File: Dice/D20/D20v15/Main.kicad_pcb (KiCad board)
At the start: 2 copper layers, 101.9 x 44.5 mm, 84 parts, among them J1 Conn_01x14, J2 Conn_01x04, J3 Conn_01x02, J4 DNP, P5 COILA, P6 COILB, U1 N52810_QFN32, U2 KXTJ3-1057, U3 PJ75AL50SA, U4 ME6215, U5 MCP73832T-2ACI/OT, U6 MT9700, U7 74AHC1G08, U8 TMR1366, Y1 32MHz 40ppm

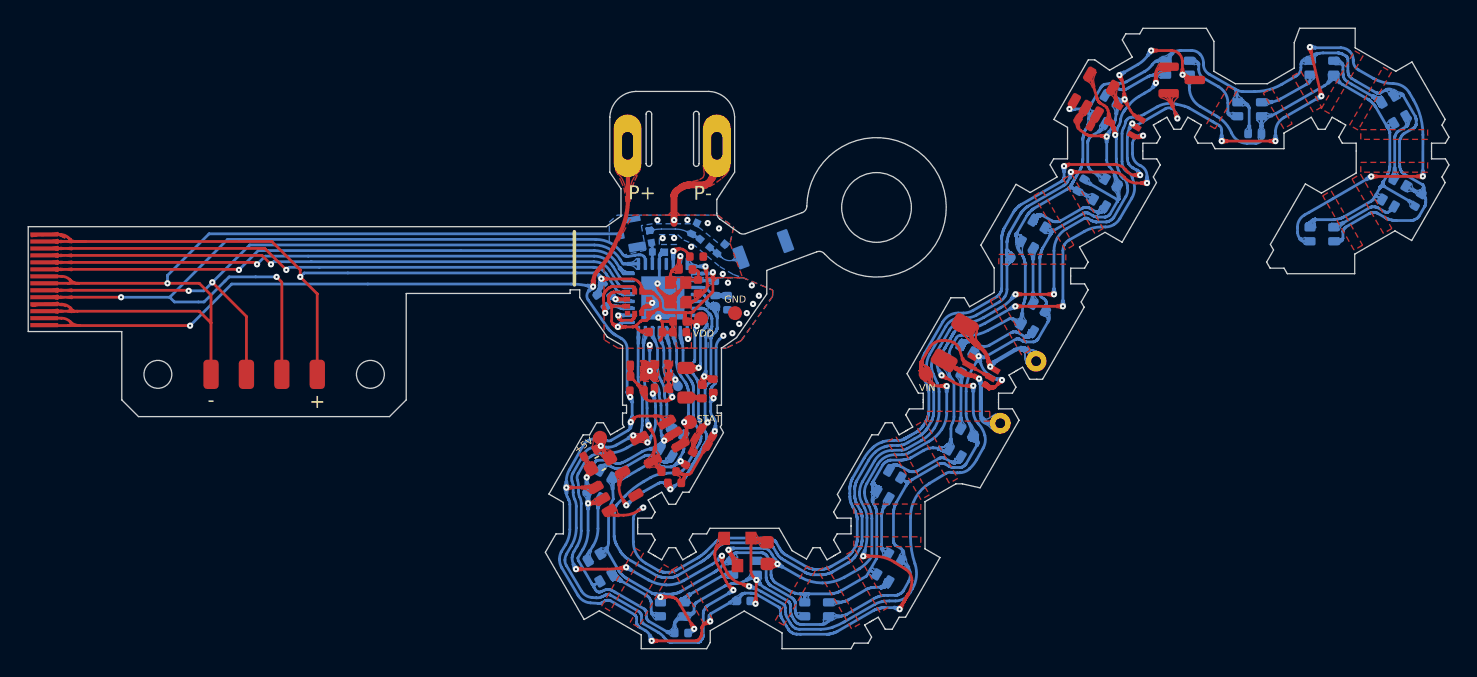
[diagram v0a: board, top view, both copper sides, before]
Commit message: Update D20V15 to include NTC over battery
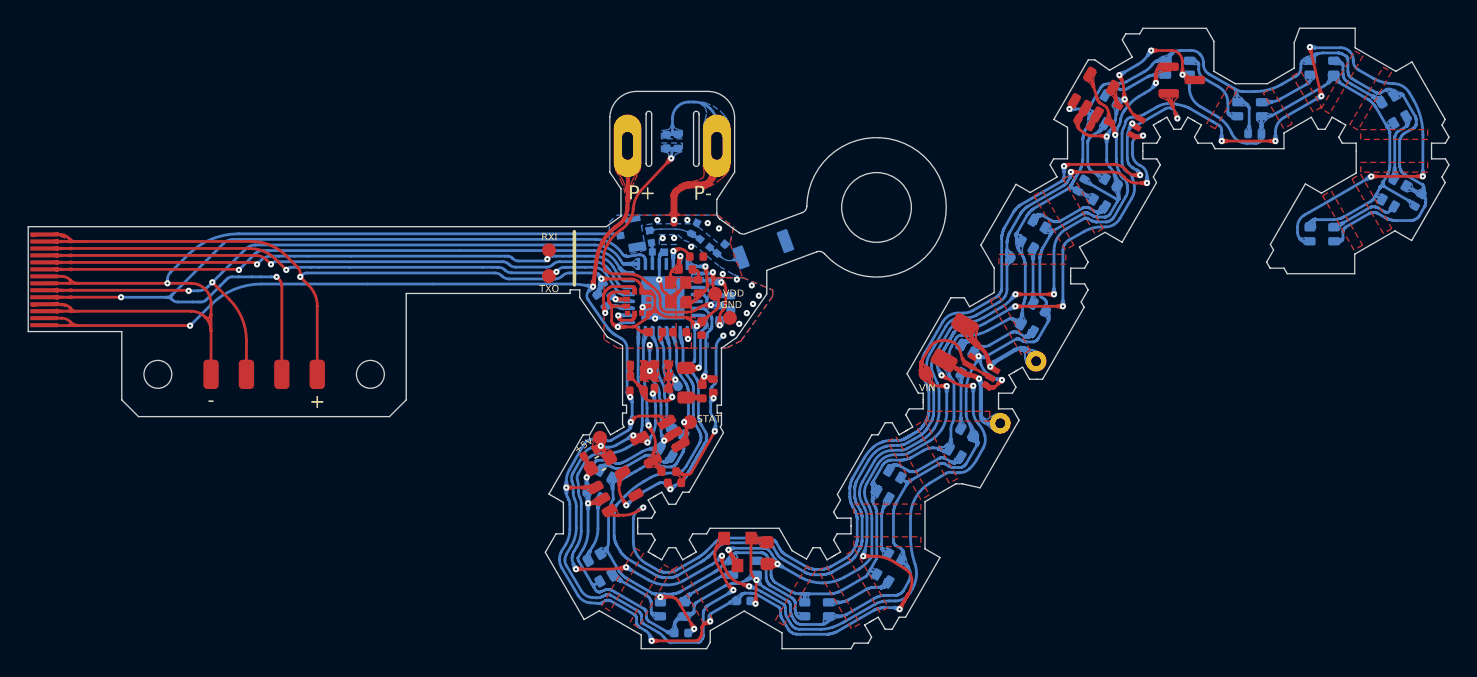
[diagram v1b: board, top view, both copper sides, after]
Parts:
- removed R13: 4.02M 1%, Pixels-dice:R_0402_1005Metric
- removed R14: 10M 1%, Pixels-dice:R_0402_1005Metric
- removed W12: VLED_S, Pixels-dice:TEST_PIN
- added R5: 100k 1%, Pixels-dice:R_0402_1005Metric, B.Cu at (145.8, 89.5)
- added TH1: NTC 100k @ 25C, Pixels-dice:R_0402_1005Metric, B.Cu at (142.8, 77.2)
- added W1: RXI, Pixels-dice:TEST_PIN, F.Cu at (133.5, 85.0)
- added W2: TXO, Pixels-dice:TEST_PIN, F.Cu at (133.5, 86.8)
- C6: value 10nF 25V 10% -> 0.1uF 10V 20%; moved to B.Cu
- moved C6 21.1 mm to (142.0, 77.2), turned to 90 degrees
- moved W25 2.04 mm to (145.5, 88.1)
- moved C4 1.64 mm to (144.5, 90.6), turned to -90 degrees
- moved W19 0.50 mm to (146.5, 89.8)
- moved R9 0.24 mm to (146.6, 88.8)
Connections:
- net /VLED_SENSE renamed /BATT_NTC
- net Net-(R10-Pad2) renamed /NTC_ID_VDD
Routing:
- net /BATT_NTC: track 12.8 -> 22.8 mm, vias 1 -> 2
- net GND: track 281.8 -> 287.9 mm
- net /NTC_ID_VDD: track 1.29 -> 4.99 mm, vias 0 -> 2
- net VDD: track 100.6 -> 99.3 mm
- net VDC: track 148.2 -> 147.4 mm, vias 4 -> 3
- net RXI: track 43.0 -> 43.1 mm, vias 1 -> 2
- net TXO: track 43.5 -> 43.6 mm, vias 1 -> 2
- added copper zone on B.Cu, net /BATT_NTC
- added copper zone on F.Cu, net /BATT_NTC
- added copper zone on B.Cu, net /NTC_ID_VDD
- added copper zone on F.Cu, net /NTC_ID_VDD
- added copper zone on B.Cu, net VDD
- added copper zone on F.Cu, net VDD

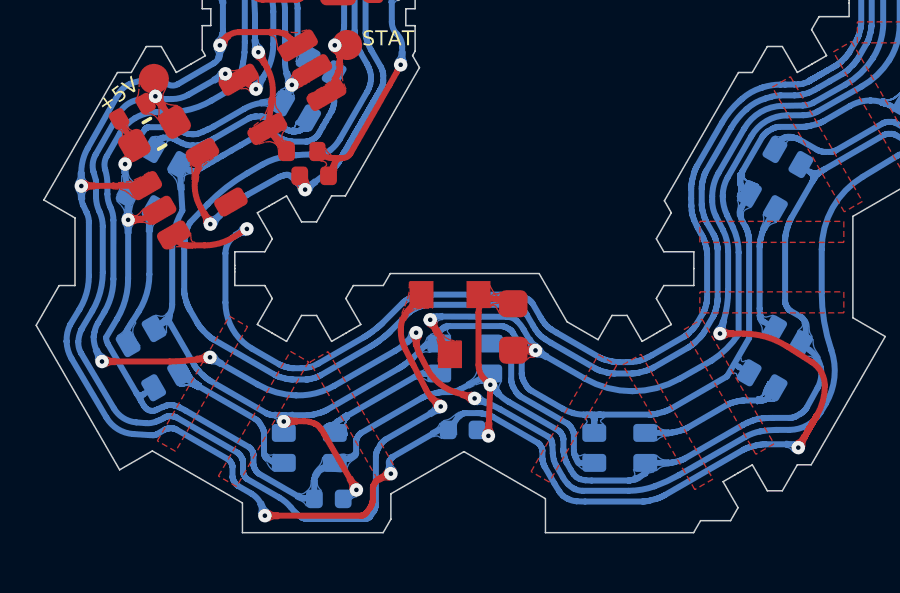
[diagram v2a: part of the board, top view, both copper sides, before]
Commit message: Updated all remaining boards to match D20V15 (D6, PD6, D8, D10 and D12)
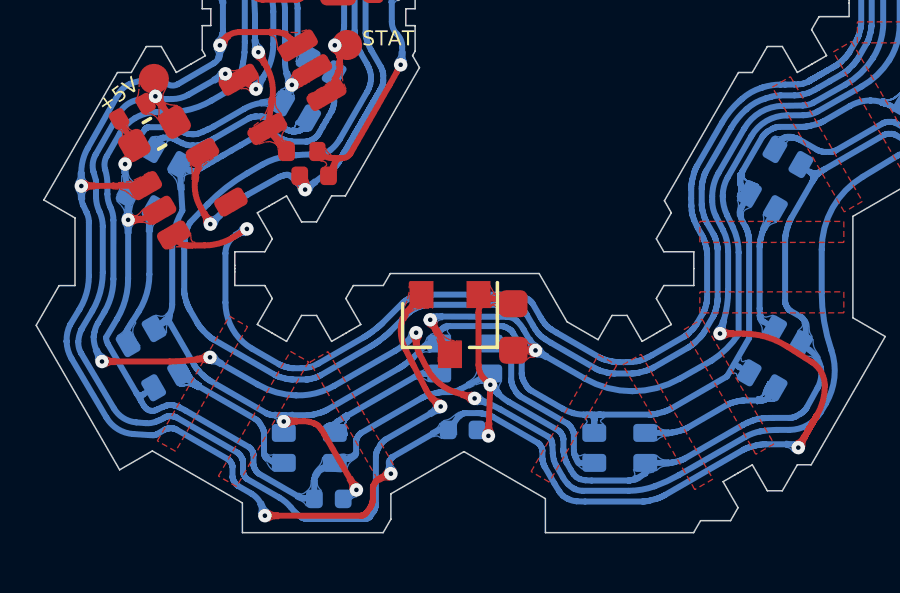
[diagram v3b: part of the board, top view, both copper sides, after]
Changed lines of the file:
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@@
       (effects (font (size 1 1) (thickness 0.15)))
     )
+    (fp_line (start -0.76 1.58) (end -0.76 0.65) (layer "F.SilkS") (width 0.12))
+    (fp_line (start -0.76 -1.58) (end -0.76 -0.65) (layer "F.SilkS") (width 0.12))
+    (fp_line (start -0.76 -1.58) (end 0.7 -1.58) (layer "F.SilkS") (width 0.12))
+    (fp_line (start -0.76 1.58) (end 1.4 1.58) (layer "F.SilkS") (width 0.12))
+    (fp_line (start 1.7 1.75) (end -1.7 1.75) (layer "F.CrtYd") (width 0.05))
+    (fp_line (start -1.7 -1.75) (end 1.7 -1.75) (layer "F.CrtYd") (width 0.05))
     (fp_line (start 1.7 -1.75) (end 1.7 1.75) (layer "F.CrtYd") (width 0.05))
     (fp_line (start -1.7 1.75) (end -1.7 -1.75) (layer "F.CrtYd") (width 0.05))
-    (fp_line (start -1.7 -1.75) (end 1.7 -1.75) (layer "F.CrtYd") (width 0.05))
-    (fp_line (start 1.7 1.75) (end -1.7 1.75) (layer "F.CrtYd") (width 0.05))
     (fp_line (start 0.15 1.52) (end -0.7 1.52) (layer "F.Fab") (width 0.1))
-    (fp_line (start -0.76 1.58) (end 1.4 1.58) (layer "F.Fab") (width 0.12))
+    (fp_line (start 0.7 -1.52) (end -0.7 -1.52) (layer "F.Fab") (width 0.1))
     (fp_line (start 0.7 0.95) (end 0.7 -1.5) (layer "F.Fab") (width 0.1))
     (fp_line (start -0.7 1.52) (end -0.7 -1.52) (layer "F.Fab") (width 0.1))
-    (fp_line (start -0.76 -1.58) (end 0.7 -1.58) (layer "F.Fab") (width 0.12))
     (fp_line (start 0.7 0.95) (end 0.15 1.52) (layer "F.Fab") (width 0.1))
-    (fp_line (start 0.7 -1.52) (end -0.7 -1.52) (layer "F.Fab") (width 0.1))
-    (fp_line (start -0.76 1.58) (end -0.76 0.65) (layer "F.Fab") (width 0.12))
-    (fp_line (start -0.76 -1.58) (end -0.76 -0.65) (layer "F.Fab") (width 0.12))
     (pad "1" smd rect (at 1 0.95 270) (size 0.9 0.8) (layers "F.Cu" "F.Paste" "F.Mask")
       (net 2 "GND") (pinfunction "VSS") (pintype "power_in"))
